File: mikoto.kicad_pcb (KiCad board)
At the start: 4 copper layers, 18 x 33.3 mm, 70 parts, among them J1 USB_C_Receptacle_USB2.0, J4 PTH, J5 PTH, U1 nRF52840, U2 BQ24075RGT, U3 XC6220B331MR, U4 mikoto-pins, U5 ESDR0502NMUTAG, Y1 32MHz, Y2 32.768 kHz

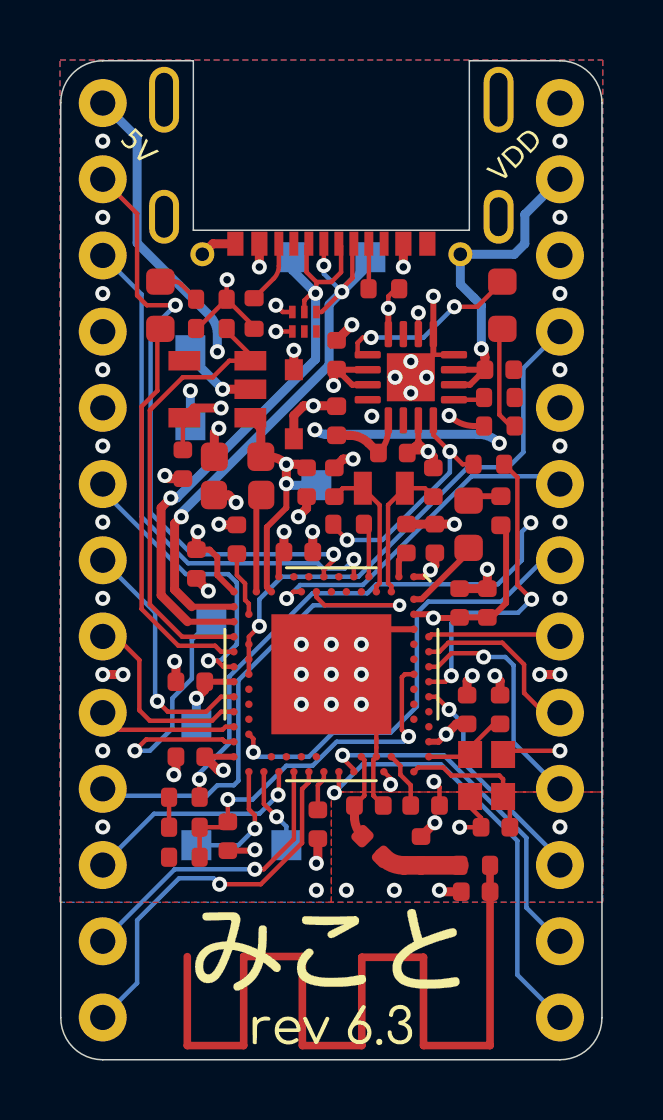
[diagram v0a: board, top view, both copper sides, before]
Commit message: rev 6.3 (for oshpark)
tweak antenna feed layout for oshpark board stackup.
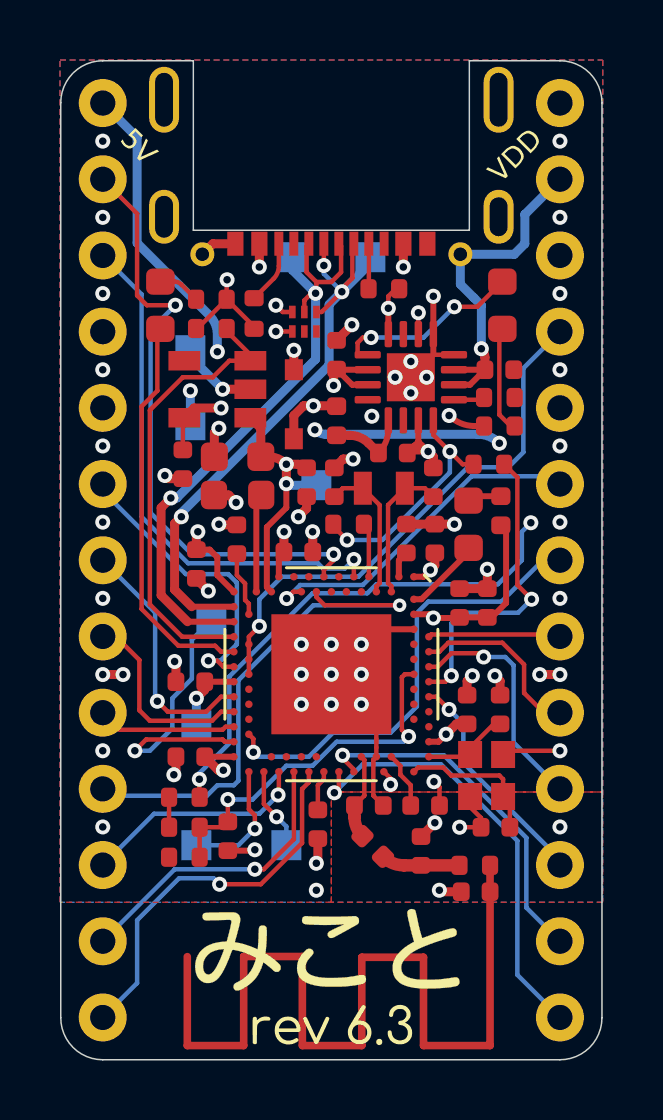
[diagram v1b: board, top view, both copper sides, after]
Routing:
- net GND: vias 65 -> 63
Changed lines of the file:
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@@
   (segment (start 1.1 7.845) (end 0.77 8.175) (width 0.15) (layer "F.Cu") (net 5))
   (segment (start 1.1 6.65) (end 1.1 7.845) (width 0.15) (layer "F.Cu") (net 5))
-  (segment (start 0.77 8.175) (end 0.77 8.552331) (width 0.3) (layer "F.Cu") (net 5))
+  (segment (start 0.77 8.175) (end 0.77 8.552331) (width 0.4141) (layer "F.Cu") (net 5))
   (segment (start 1 6.55) (end 1.1 6.65) (width 0.15) (layer "F.Cu") (net 5))
-  (arc (start 0.77 8.552331) (mid 0.839405 8.901252) (end 1.037053 9.197053) (width 0.3) (layer "F.Cu") (net 5))
+  (arc (start 0.77 8.552331) (mid 0.839405 8.901252) (end 1.037053 9.197053) (width 0.4141) (layer "F.Cu") (net 5))
   (segment (start 2.25 0.005) (end 2.5 -0.245) (width 0.2) (layer "F.Cu") (net 6))
   (segment (start 2.25 0.55) (end 2.25 0.005) (width 0.2) (layer "F.Cu") (net 6))
@@
   (segment (start 4.1 -8.45) (end 3.075 -7.425) (width 0.15) (layer "B.Cu") (net 17))
   (segment (start 3.075 -7.425) (end 1.325 -7.425) (width 0.15) (layer "B.Cu") (net 17))
-  (segment (start 2.415954 10.17) (end 2.99 10.17) (width 0.6199) (layer "F.Cu") (net 18))
-  (segment (start 2.99 10.17) (end 4.27 10.17) (width 0.6199) (layer "F.Cu") (net 18))
-  (arc (start 1.722947 9.882947) (mid 2.040901 10.095397) (end 2.415954 10.17) (width 0.6199) (layer "F.Cu") (net 18))
+  (segment (start 2.415954 10.17) (end 2.99 10.17) (width 0.4141) (layer "F.Cu") (net 18))
+  (segment (start 2.99 10.17) (end 4.27 10.17) (width 0.4141) (layer "F.Cu") (net 18))
+  (arc (start 1.722947 9.882947) (mid 2.040901 10.095397) (end 2.415954 10.17) (width 0.4141) (layer "F.Cu") (net 18))
   (segment (start 0 -9.275) (end 0.325 -9.6) (width 0.15) (layer "F.Cu") (net 19))
   (segment (start -0.6625 -8.9) (end -0.9 -8.6625) (width 0.15) (layer "F.Cu") (net 19))
@@
   (via (at -3.475 -9.35) (size 0.5) (drill 0.25) (layers "F.Cu" "B.Cu") (net 39))
   (via (at 0 3.8) (size 0.5) (drill 0.25) (layers "F.Cu" "B.Cu") (net 39))
-  (via (at 0.5 11) (size 0.5) (drill 0.25) (layers "F.Cu" "B.Cu") (net 39))
   (via locked (at -7.62 6.35) (size 0.5) (drill 0.25) (layers "F.Cu" "B.Cu") (net 39))
   (via locked (at 7.62 -3.81) (size 0.5) (drill 0.25) (layers "F.Cu" "B.Cu") (net 39))
@@
   (via (at 3.175 -6.1) (size 0.5) (drill 0.25) (layers "F.Cu" "B.Cu") (net 39))
   (via (at 3.42 7.38) (size 0.5) (drill 0.25) (layers "F.Cu" "B.Cu") (net 39))
-  (via (at 2.1 11) (size 0.5) (drill 0.25) (layers "F.Cu" "B.Cu") (free) (net 39))
   (via locked (at 7.62 -13.97) (size 0.5) (drill 0.25) (layers "F.Cu" "B.Cu") (net 39))
   (via locked (at 7.62 8.89) (size 0.5) (drill 0.25) (layers "F.Cu" "B.Cu") (net 39))
@@
   )
   (zone locked (net 39) (net_name "GND") (layer "F.Cu") (hatch edge 0.508)
-    (connect_pads thru_hole_only (clearance 0.125))
-    (min_thickness 0.125) (filled_areas_thickness no)
-    (fill yes (thermal_gap 0.125) (thermal_bridge_width 0.6))
+    (connect_pads thru_hole_only (clearance 0.15))
+    (min_thickness 0.15) (filled_areas_thickness no)
+    (fill yes (thermal_gap 0.15) (thermal_bridge_width 0.6))
     (polygon
       (pts
@@
     )
   )
+  (zone (net 0) (net_name "") (layer "F.Cu") (hatch edge 0.508)
+    (connect_pads thru_hole_only (clearance 0))
+    (min_thickness 0.15)
+    (keepout (tracks allowed) (vias allowed) (pads allowed ) (copperpour not_allowed) (footprints allowed))
+    (fill (thermal_gap 0.15) (thermal_bridge_width 0.6))
+    (polygon
+      (pts
+        (xy 9.045 11.4)
+        (xy 0 11.4)
+        (xy 0 7.725)
+        (xy 9.045 7.725)
+      )
+    )
+  )
   (zone locked (net 0) (net_name "") (layer "F.Cu") (hatch edge 0.508)
     (connect_pads (clearance 0))
@@
     (keepout (tracks allowed) (vias allowed) (pads allowed ) (copperpour not_allowed) (footprints allowed))
     (fill (thermal_gap 0.2) (thermal_bridge_width 0.508))
+  )
+  (zone locked (net 0) (net_name "") (layers "F.Cu" "In1.Cu" "In2.Cu" "B.Cu") (hatch edge 0.508)
+    (connect_pads thru_hole_only (clearance 0))
+    (min_thickness 0.15)
+    (keepout (tracks allowed) (vias allowed) (pads allowed ) (copperpour not_allowed) (footprints allowed))
+    (fill (thermal_gap 0.15) (thermal_bridge_width 0.6))
+    (polygon
+      (pts
+        (xy 6.25 -10.7)
+        (xy 5.95 -10.4)
+        (xy 5 -10.4)
+        (xy 4.375 -11.025)
+        (xy -4.375 -11.025)
+        (xy -5 -10.4)
+        (xy -5.95 -10.4)
+        (xy -6.25 -10.7)
+        (xy -6.25 -16.675)
+        (xy 6.25 -16.675)
+      )
+    )
   )
   (zone locked (net 0) (net_name "") (layer "F.Cu") (hatch edge 0.508)
@@
     (connect_pads (clearance 0))
     (min_thickness 0.254)
-    (keepout (tracks allowed) (vias allowed) (pads allowed ) (copperpour not_allowed) (footprints allowed))
+    (keepout (tracks allowed) (vias allowed) (pads allowed ) (copperpour allowed) (footprints allowed))
     (fill (thermal_gap 0.508) (thermal_bridge_width 0.508))
     (polygon
